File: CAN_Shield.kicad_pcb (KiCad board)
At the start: 2 copper layers, 65 x 56.5 mm, 27 parts, among them J1 GPIO, U1 ATECC608A-SSHDA-T, U2 MCP2515T-I/SO, U4 SN65HVD230DR, X1 X322516MLB4SI, j2 DB128V-5.08-5P-GN-S, j3 DB128V-5.08-7P-GN-S, j4 DB128V-5.08-7P-GN-S

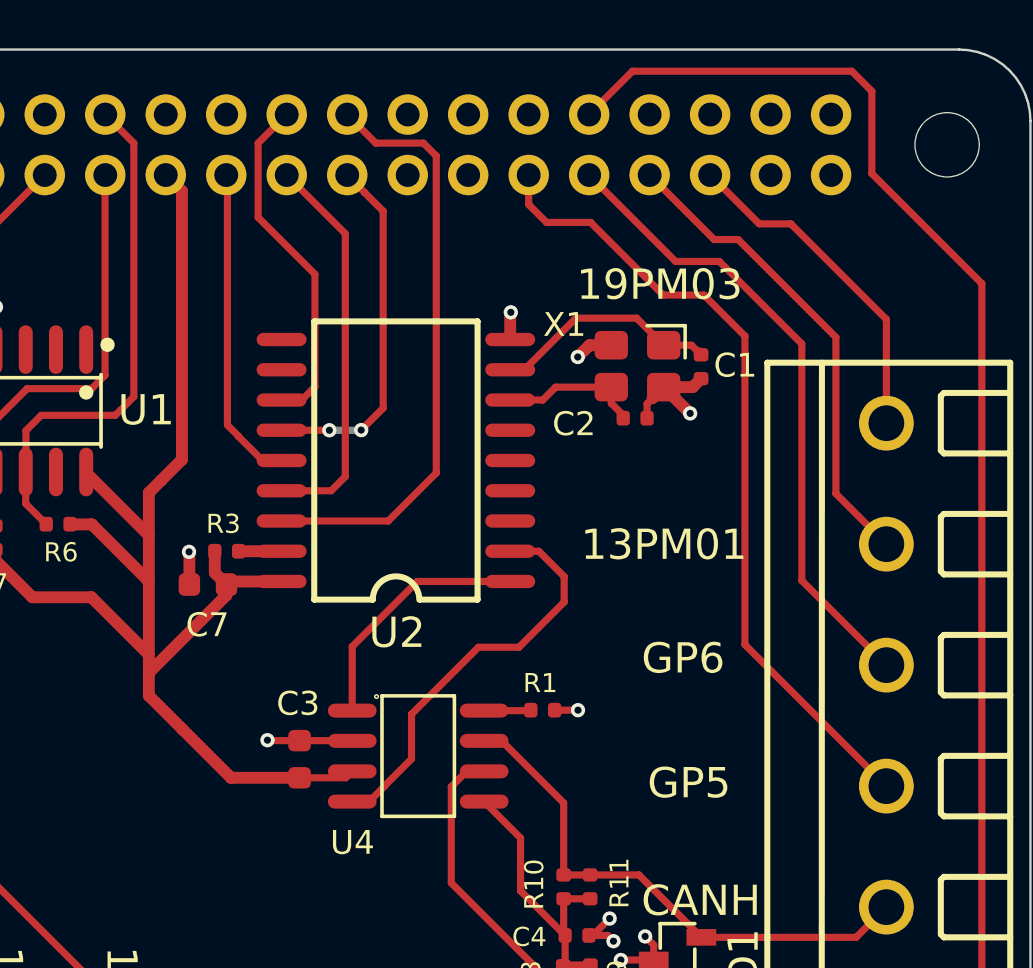
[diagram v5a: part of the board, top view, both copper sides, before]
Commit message: add both bulk and bypass cap for sn65, increase spaing for crystal and add guard trace for crystal
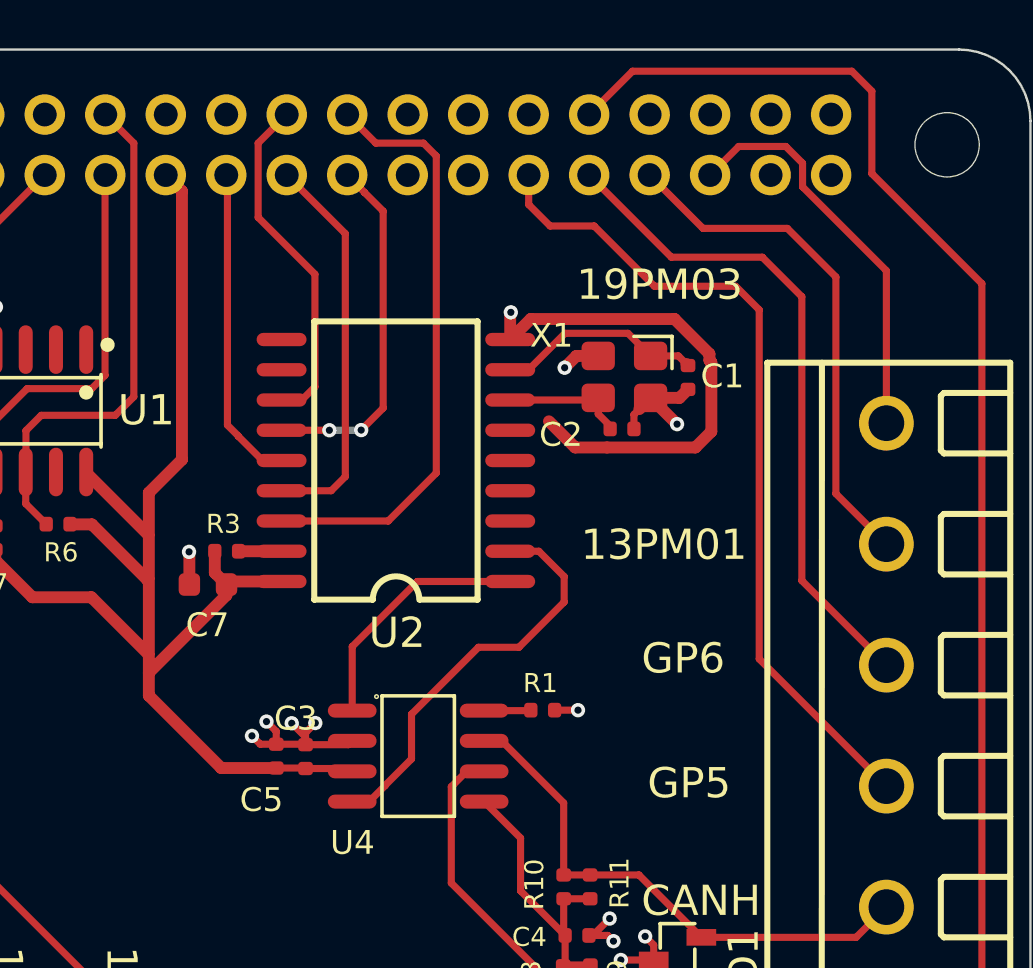
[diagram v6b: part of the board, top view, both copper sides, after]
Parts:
- added C5: 100nF, PCM_JLCPCB:C_0402, F.Cu at (133.3, 73.2)
- C3: value 100nF -> 10nF; footprint PCM_JLCPCB:C_0603 -> PCM_JLCPCB:C_0402
- moved C2 0.71 mm to (147.8, 59.4)
- moved C1 0.71 mm to (150.6, 57.3)
- moved X1 0.71 mm to (147.9, 57.2)
- moved C3 0.27 mm to (134.6, 73.2)
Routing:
- net GND: track 21.3 -> 45.5 mm, vias 11 -> 14
- net /GPIO19/PCM.FS: track 14.9 -> 17.7 mm
- net /GPIO13/PWM1: track 20.2 -> 21.7 mm
- net /GPIO6: track 26.8 -> 28.0 mm
- net /GPIO5: track 34.0 -> 35.0 mm
- net /OSC1: track 9.65 -> 8.76 mm
- net /OSC2: track 5.99 -> 5.41 mm
- net +3V3: track 74.3 -> 73.7 mm

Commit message: recheck to add all change
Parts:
- moved G*** 45.2 mm to (126.1, 73.1)
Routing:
- net GND: track 45.5 -> 45.9 mm, vias 14 -> 21
